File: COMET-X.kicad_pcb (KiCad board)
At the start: 2 copper layers, 110 x 45 mm, 19 parts, among them J1 ATX_12V_IN, J2 10146065-113Y1LF, J3 G97R24312HR_EP, U2 TPS5450ddar

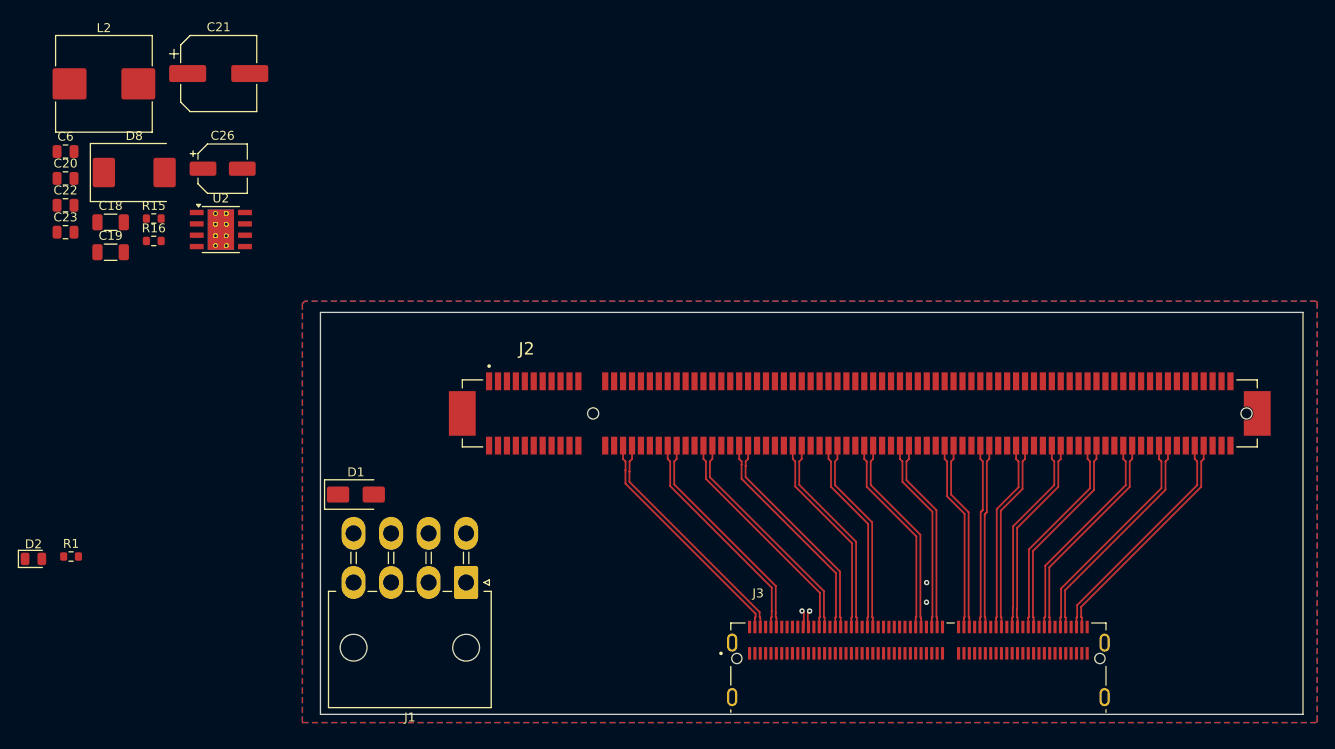
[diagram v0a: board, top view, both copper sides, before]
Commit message: updated stackup and regulator
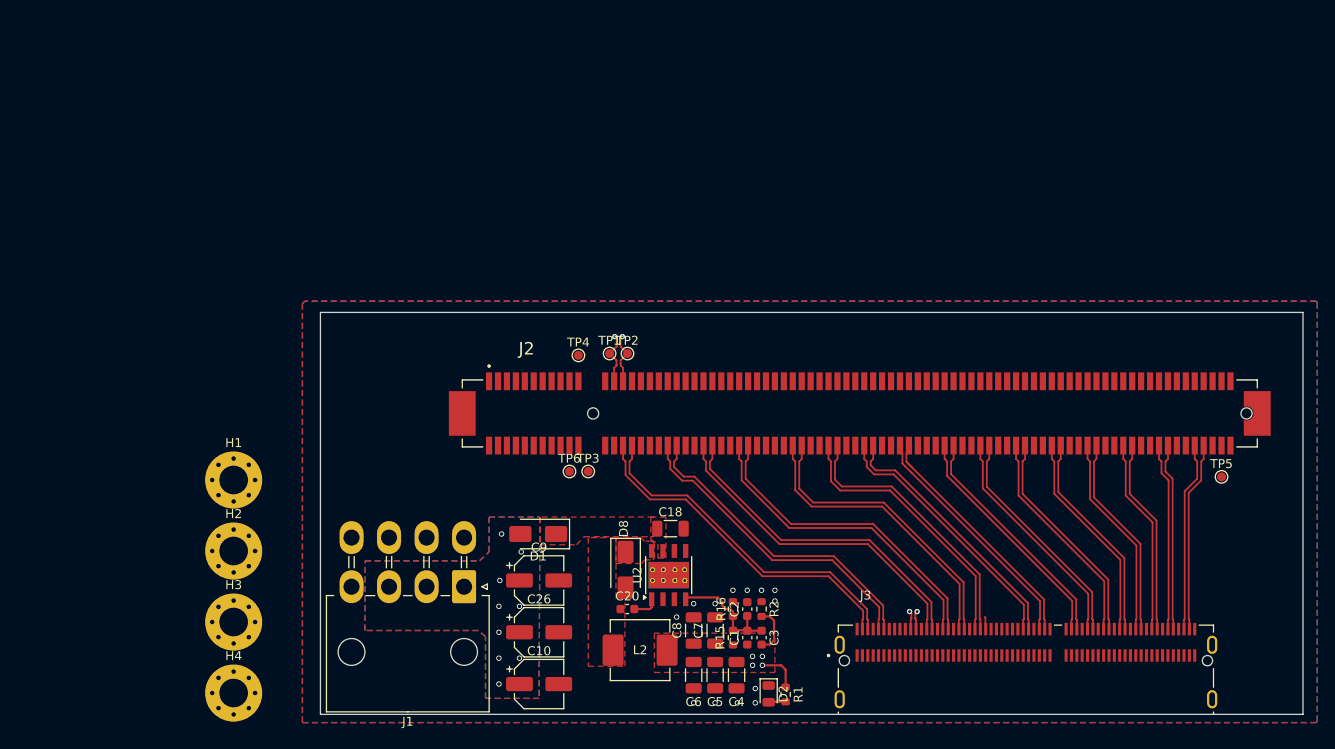
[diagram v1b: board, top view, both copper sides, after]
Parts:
- removed C19: 22u, Capacitor_SMD:C_1206_3216Metric
- removed C21: 220u, Capacitor_SMD:CP_Elec_8x11.9
- removed C22: 100n, Capacitor_SMD:C_0805_2012Metric
- removed C23: 10n, Capacitor_SMD:C_0805_2012Metric
- added C1: ~, Capacitor_SMD:C_0603_1608Metric, F.Cu at (156.3, 108.0)
- added C10: 10u/50V, Capacitor_SMD:CP_Elec_5x5.4, F.Cu at (133.0, 113.2)
- added C2: ~, Capacitor_SMD:C_0603_1608Metric, F.Cu at (156.3, 104.8)
- added C3: ~, Capacitor_SMD:C_0603_1608Metric, F.Cu at (157.9, 108.0)
- added C4: 22u, Capacitor_SMD:C_1206_3216Metric, F.Cu at (155.1, 112.2)
- added C5: 22u, Capacitor_SMD:C_1206_3216Metric, F.Cu at (152.7, 112.2)
- added C7: 22u, Capacitor_SMD:C_1206_3216Metric, F.Cu at (152.7, 107.2)
- added C8: 22u, Capacitor_SMD:C_1206_3216Metric, F.Cu at (150.3, 107.2)
- added C9: 10u/50V, Capacitor_SMD:CP_Elec_5x5.4, F.Cu at (133.0, 101.6)
- added H1: ~, MountingHole:MountingHole_3.2mm_M3_Pad_Via, F.Cu at (98.8, 90.4)
- added H2: ~, MountingHole:MountingHole_3.2mm_M3_Pad_Via, F.Cu at (98.8, 98.3)
- added H3: ~, MountingHole:MountingHole_3.2mm_M3_Pad_Via, F.Cu at (98.8, 106.3)
- added H4: ~, MountingHole:MountingHole_3.2mm_M3_Pad_Via, F.Cu at (98.8, 114.2)
- added R2: ~, Resistor_SMD:R_0603_1608Metric, F.Cu at (157.9, 104.8)
- added TP1: CLK_P, TestPoint:TestPoint_Pad_D1.0mm, F.Cu at (140.9, 76.2)
- added TP2: CLK_N, TestPoint:TestPoint_Pad_D1.0mm, F.Cu at (142.9, 76.2)
- added TP3: WAKE, TestPoint:TestPoint_Pad_D1.0mm, F.Cu at (138.5, 89.4)
- added TP4: PERST, TestPoint:TestPoint_Pad_D1.0mm, F.Cu at (137.4, 76.4)
- added TP5: PRES, TestPoint:TestPoint_Pad_D1.0mm, F.Cu at (209.4, 90.0)
- added TP6: 3V3_AUX, TestPoint:TestPoint_Pad_D1.0mm, F.Cu at (136.4, 89.4)
- C20: footprint Capacitor_SMD:C_0805_2012Metric -> Capacitor_SMD:C_0603_1608Metric
- C6: value 100n -> 22u; footprint Capacitor_SMD:C_0805_2012Metric -> Capacitor_SMD:C_1206_3216Metric
- D8: value SSC54-E3/9AT -> SS54; footprint Diode_SMD:D_SMC -> Diode_SMD:D_SMA
- L2: value TBD -> 10uH; footprint Inductor_SMD:L_Wuerth_HCI-1030 -> Inductor_SMD:L_Changjiang_FXL0630
- R15: value TBD -> 10k
- R16: value TBD -> 5.9k
- moved C6 91.6 mm to (150.3, 112.2), turned to -90 degrees
- moved L2 87.3 mm to (144.3, 109.4)
- moved D2 83.7 mm to (158.7, 114.3), turned to -90 degrees
- moved R1 81.5 mm to (160.6, 114.4), turned to -90 degrees
- moved R15 80.0 mm to (154.7, 108.0), turned to 90 degrees
- moved C20 79.3 mm to (142.9, 104.8)
- moved R16 76.8 mm to (154.7, 104.8), turned to 90 degrees
- moved C18 71.4 mm to (147.7, 95.8)
- moved D8 70.7 mm to (142.7, 100.4), turned to -90 degrees
- moved U2 63.3 mm to (147.5, 101.0), turned to 90 degrees
- moved C26 62.8 mm to (133.0, 107.4)
- moved D1 20.9 mm to (132.9, 96.4), turned to 180 degrees
- moved J3 12.0 mm to (187.5, 110.6)
- moved J1 0.53 mm to (124.6, 102.3)
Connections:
- C18 pad 1: Net-(D1-K) -> VBUS
- C26 pad 1: Net-(D1-K) -> +12V
- C6 pad 1: Net-(D1-K) -> +3V3
- D1 pad 1: Net-(D1-K) -> VBUS
- U2 pad 7: Net-(D1-K) -> VBUS
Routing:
- net CLK_P: track 1.90 -> 58.0 mm, vias 1 -> 2
- net CLK_N: track 1.90 -> 58.0 mm, vias 1 -> 2
- net /VSENS: track 0.00 -> 13.2 mm
- net TX0_N: track 26.5 -> 38.4 mm
- net TX0_P: track 26.5 -> 38.4 mm
- net TX2_N: track 25.7 -> 36.8 mm
- net TX2_P: track 25.7 -> 36.8 mm
- net TX3_N: track 24.8 -> 35.4 mm
- net TX3_P: track 24.8 -> 35.4 mm
- net TX4_N: track 23.1 -> 32.9 mm
- net TX4_P: track 23.1 -> 32.9 mm
- net TX1_P: track 25.2 -> 35.0 mm
- net TX1_N: track 25.2 -> 35.0 mm
- net TX5_P: track 22.2 -> 30.7 mm
- net TX5_N: track 22.2 -> 30.7 mm
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- added copper zone on B.Cu, net +12V
- added copper zone on F.Cu, net +12V
- added copper zone on F.Cu, net +3V3
- added copper zone on In1.Cu, net GND
- added copper zone on In2.Cu, net GND
- added copper zone on In3.Cu, net GND
- added copper zone on In4.Cu, net GND
- added copper zone on F.Cu, net Net-(D8-K)
- added copper zone on F.Cu, net VBUS
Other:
- copper layers 2 -> 6
